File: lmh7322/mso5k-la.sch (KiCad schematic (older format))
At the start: 4 parts, among them J1 output, J2 input

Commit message: Minor cleanup
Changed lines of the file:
@@
 Wire Wire Line
 	3650 4450 3800 4450
-Text GLabel 4550 4400 0    50   Input ~ 0
+Text GLabel 4500 4400 0    50   Input ~ 0
 In8
-Text GLabel 4550 4550 0    50   Input ~ 0
+Text GLabel 4500 4550 0    50   Input ~ 0
 In9
 Wire Wire Line
-	4550 4400 4700 4400
-Wire Wire Line
-	4550 4550 4700 4550
-Text GLabel 4550 5700 0    50   Input ~ 0
+	4500 4400 4650 4400
+Wire Wire Line
+	4500 4550 4650 4550
+Text GLabel 4500 5700 0    50   Input ~ 0
 In10
-Text GLabel 4550 5850 0    50   Input ~ 0
+Text GLabel 4500 5850 0    50   Input ~ 0
 In11
 Wire Wire Line
-	4700 5700 4550 5700
-Wire Wire Line
-	4700 5850 4550 5850
-Text GLabel 5400 4700 2    50   Input ~ 0
+	4650 5700 4500 5700
+Wire Wire Line
+	4650 5850 4500 5850
+Text GLabel 5350 4700 2    50   Input ~ 0
 D9
-Text GLabel 5400 4800 2    50   Input ~ 0
+Text GLabel 5350 4800 2    50   Input ~ 0
 ~D9
-Text GLabel 5400 4450 2    50   Input ~ 0
+Text GLabel 5350 4450 2    50   Input ~ 0
 D8
-Text GLabel 5400 4550 2    50   Input ~ 0
+Text GLabel 5350 4550 2    50   Input ~ 0
 ~D8
-Text GLabel 5400 6000 2    50   Input ~ 0
+Text GLabel 5350 6000 2    50   Input ~ 0
 D11
-Text GLabel 5400 6100 2    50   Input ~ 0
+Text GLabel 5350 6100 2    50   Input ~ 0
 ~D11
-Text GLabel 5400 5750 2    50   Input ~ 0
+Text GLabel 5350 5750 2    50   Input ~ 0
 D10
-Text GLabel 5400 5850 2    50   Input ~ 0
+Text GLabel 5350 5850 2    50   Input ~ 0
 ~D10
 Wire Wire Line
-	5400 6100 5250 6100
-Wire Wire Line
-	5250 6000 5400 6000
-Wire Wire Line
-	5400 5850 5250 5850
-Wire Wire Line
-	5250 5750 5400 5750
-Wire Wire Line
-	5400 4800 5250 4800
-Wire Wire Line
-	5250 4700 5400 4700
-Wire Wire Line
-	5400 4550 5250 4550
-Wire Wire Line
-	5250 4450 5400 4450
-Text GLabel 6350 4400 0    50   Input ~ 0
+	5350 6100 5200 6100
+Wire Wire Line
+	5200 6000 5350 6000
+Wire Wire Line
+	5350 5850 5200 5850
+Wire Wire Line
+	5200 5750 5350 5750
+Wire Wire Line
+	5350 4800 5200 4800
+Wire Wire Line
+	5200 4700 5350 4700
+Wire Wire Line
+	5350 4550 5200 4550
+Wire Wire Line
+	5200 4450 5350 4450
+Text GLabel 6050 4400 0    50   Input ~ 0
 In12
-Text GLabel 6350 4550 0    50   Input ~ 0
+Text GLabel 6050 4550 0    50   Input ~ 0
 In13
 Wire Wire Line
-	6350 4400 6500 4400
-Wire Wire Line
-	6350 4550 6500 4550
-Text GLabel 6350 5700 0    50   Input ~ 0
+	6050 4400 6200 4400
+Wire Wire Line
+	6050 4550 6200 4550
+Text GLabel 6050 5700 0    50   Input ~ 0
 In14
-Text GLabel 6350 5850 0    50   Input ~ 0
+Text GLabel 6050 5850 0    50   Input ~ 0
 In15
 Wire Wire Line
-	6500 5700 6350 5700
-Wire Wire Line
-	6500 5850 6350 5850
-Text GLabel 7200 4700 2    50   Input ~ 0
+	6200 5700 6050 5700
+Wire Wire Line
+	6200 5850 6050 5850
+Text GLabel 6900 4700 2    50   Input ~ 0
 D13
-Text GLabel 7200 4800 2    50   Input ~ 0
+Text GLabel 6900 4800 2    50   Input ~ 0
 ~D13
-Text GLabel 7200 4450 2    50   Input ~ 0
+Text GLabel 6900 4450 2    50   Input ~ 0
 D12
-Text GLabel 7200 4550 2    50   Input ~ 0
+Text GLabel 6900 4550 2    50   Input ~ 0
 ~D12
-Text GLabel 7200 6000 2    50   Input ~ 0
+Text GLabel 6900 6000 2    50   Input ~ 0
 D15
-Text GLabel 7200 6100 2    50   Input ~ 0
+Text GLabel 6900 6100 2    50   Input ~ 0
 ~D15
-Text GLabel 7200 5750 2    50   Input ~ 0
+Text GLabel 6900 5750 2    50   Input ~ 0
 D14
-Text GLabel 7200 5850 2    50   Input ~ 0
+Text GLabel 6900 5850 2    50   Input ~ 0
 ~D14
 Wire Wire Line
-	7200 6100 7050 6100
-Wire Wire Line
-	7050 6000 7200 6000
-Wire Wire Line
-	7200 5850 7050 5850
-Wire Wire Line
-	7050 5750 7200 5750
-Wire Wire Line
-	7200 4800 7050 4800
-Wire Wire Line
-	7050 4700 7200 4700
-Wire Wire Line
-	7200 4550 7050 4550
-Wire Wire Line
-	7050 4450 7200 4450
+	6900 6100 6750 6100
+Wire Wire Line
+	6750 6000 6900 6000
+Wire Wire Line
+	6900 5850 6750 5850
+Wire Wire Line
+	6750 5750 6900 5750
+Wire Wire Line
+	6900 4800 6750 4800
+Wire Wire Line
+	6750 4700 6900 4700
+Wire Wire Line
+	6900 4550 6750 4550
+Wire Wire Line
+	6750 4450 6900 4450
 Text GLabel 1450 6050 0    50   Input ~ 0
 Vref_0-7
@@
 Wire Wire Line
 	3100 6050 2950 6050
-Text GLabel 4550 6050 0    50   Input ~ 0
+Text GLabel 4500 6050 0    50   Input ~ 0
 Vref_8-15
-Text GLabel 6350 6050 0    50   Input ~ 0
+Text GLabel 6050 6050 0    50   Input ~ 0
 Vref_8-15
 Wire Wire Line
-	6350 6050 6500 6050
-Wire Wire Line
-	4700 6050 4550 6050
+	6050 6050 6200 6050
+Wire Wire Line
+	4650 6050 4500 6050
 Text Notes 1050 3950 0    50   ~ 0
 For reference see:\nhttp://www.eevblog.com/forum/testgear/hacking-the-rigol-mso5000-series-oscilloscopes/msg2057401/#msg2057401
@@
 $EndSheet
 $Sheet
-S 4700 5600 550  650
+S 4650 5600 550  650
 U 5C4E2524
 F0 "ch 10-11" 50
 F1 "dual.sch" 50
-F2 "InB" I L 4700 5850 50
-F3 "Vref" I L 4700 6050 50
-F4 "OutA" I R 5250 5750 50
-F5 "~OutA" I R 5250 5850 50
-F6 "InA" I L 4700 5700 50
-F7 "OutB" I R 5250 6000 50
-F8 "~OutB" I R 5250 6100 50
-$EndSheet
-$Sheet
-S 4700 4300 550  650
+F2 "InB" I L 4650 5850 50
+F3 "Vref" I L 4650 6050 50
+F4 "OutA" I R 5200 5750 50
+F5 "~OutA" I R 5200 5850 50
+F6 "InA" I L 4650 5700 50
+F7 "OutB" I R 5200 6000 50
+F8 "~OutB" I R 5200 6100 50
+$EndSheet
+$Sheet
+S 4650 4300 550  650
 U 5C4E98BE
 F0 "ch 8-9" 50
 F1 "dual.sch" 50
-F2 "InB" I L 4700 4550 50
-F3 "Vref" I L 4700 4750 50
-F4 "OutA" I R 5250 4450 50
-F5 "~OutA" I R 5250 4550 50
-F6 "InA" I L 4700 4400 50
-F7 "OutB" I R 5250 4700 50
-F8 "~OutB" I R 5250 4800 50
-$EndSheet
-$Sheet
-S 6500 4300 550  650
+F2 "InB" I L 4650 4550 50
+F3 "Vref" I L 4650 4750 50
+F4 "OutA" I R 5200 4450 50
+F5 "~OutA" I R 5200 4550 50
+F6 "InA" I L 4650 4400 50
+F7 "OutB" I R 5200 4700 50
+F8 "~OutB" I R 5200 4800 50
+$EndSheet
+$Sheet
+S 6200 4300 550  650
 U 5C4E98C7
 F0 "ch 12-13" 50
 F1 "dual.sch" 50
-F2 "InB" I L 6500 4550 50
-F3 "Vref" I L 6500 4750 50
-F4 "OutA" I R 7050 4450 50
-F5 "~OutA" I R 7050 4550 50
-F6 "InA" I L 6500 4400 50
-F7 "OutB" I R 7050 4700 50
-F8 "~OutB" I R 7050 4800 50
-$EndSheet
-$Sheet
-S 6500 5600 550  650
+F2 "InB" I L 6200 4550 50
+F3 "Vref" I L 6200 4750 50
+F4 "OutA" I R 6750 4450 50
+F5 "~OutA" I R 6750 4550 50
+F6 "InA" I L 6200 4400 50
+F7 "OutB" I R 6750 4700 50
+F8 "~OutB" I R 6750 4800 50
+$EndSheet
+$Sheet
+S 6200 5600 550  650
 U 5C4E98D0
 F0 "ch 14-15" 50
 F1 "dual.sch" 50
-F2 "InB" I L 6500 5850 50
-F3 "Vref" I L 6500 6050 50
-F4 "OutA" I R 7050 5750 50
-F5 "~OutA" I R 7050 5850 50
-F6 "InA" I L 6500 5700 50
-F7 "OutB" I R 7050 6000 50
-F8 "~OutB" I R 7050 6100 50
+F2 "InB" I L 6200 5850 50
+F3 "Vref" I L 6200 6050 50
+F4 "OutA" I R 6750 5750 50
+F5 "~OutA" I R 6750 5850 50
+F6 "InA" I L 6200 5700 50
+F7 "OutB" I R 6750 6000 50
+F8 "~OutB" I R 6750 6100 50
 $EndSheet
 Text GLabel 2950 4750 0    50   Input ~ 0
@@
 Wire Wire Line
 	2950 4750 3100 4750
-Text GLabel 4550 4750 0    50   Input ~ 0
+Text GLabel 4500 4750 0    50   Input ~ 0
 Vref_8-15
 Wire Wire Line
-	4550 4750 4700 4750
-Text GLabel 6350 4750 0    50   Input ~ 0
+	4500 4750 4650 4750
+Text GLabel 6050 4750 0    50   Input ~ 0
 Vref_8-15
 Wire Wire Line
-	6350 4750 6500 4750
+	6050 4750 6200 4750
 $EndSCHEMATC

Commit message: Started playing around with the PCB layout
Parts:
- added C13, C14, C15: 10uF, Capacitors_SMD.pretty:C_1206_HandSoldering, symbol Device:C
- added C16: 100n, Capacitors_SMD.pretty:C_0603_HandSoldering, symbol Device:C
- J1: footprint (none) -> Connectors_IDC.pretty:IDC-Header_2x25_Pitch2.54mm_Angled
- J2: footprint (none) -> Connector_PinHeader_2.54mm:PinHeader_1x17_P2.54mm_Horizontal
- R1, R2: footprint (none) -> Resistor_SMD:R_0603_1608Metric_Pad1.05x0.95mm_HandSolder
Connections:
- net +2V5: now also C14.1
- net +4V: now also C13.1
- net -2V5: now also C15.1
- net GND: now also C13.2, C14.2, C15.2, C16.2
- new net Vref: C16.1
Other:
- moved on the sheet: R1, R2

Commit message: Pre-clone
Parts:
- renumbered C13 to C101, C14 to C102, C15 to C103, C16 to C104, J1 to J101, J2 to J102, R1 to R101, R2 to R102

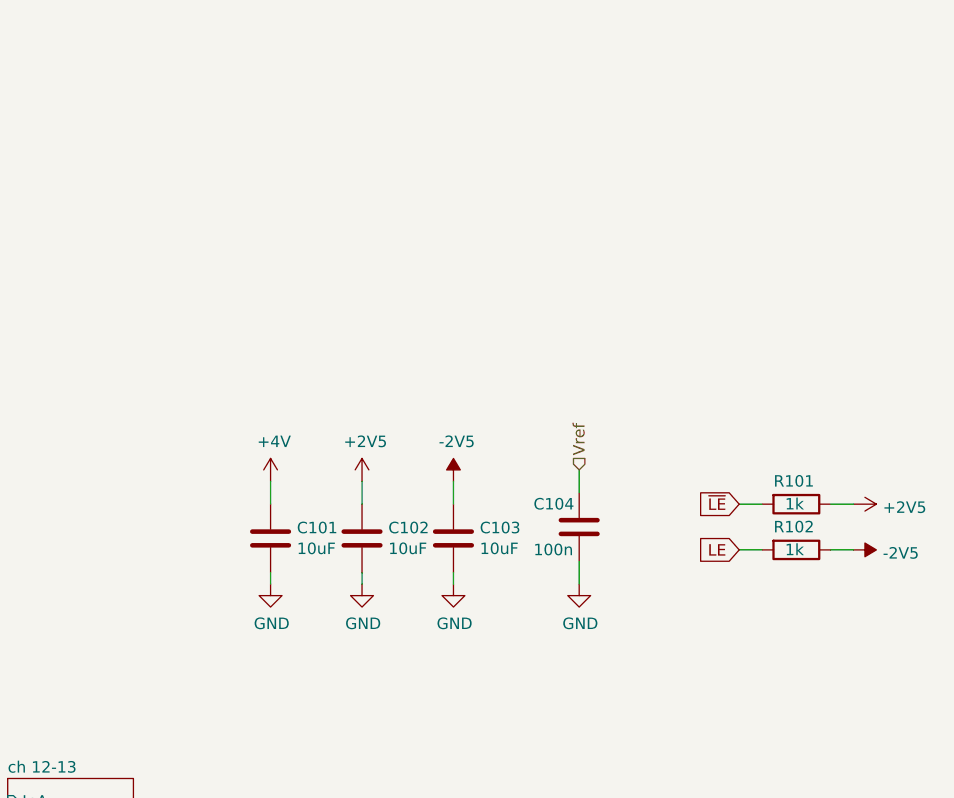
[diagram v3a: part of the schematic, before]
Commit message: Finished the 4-layer single-sided board
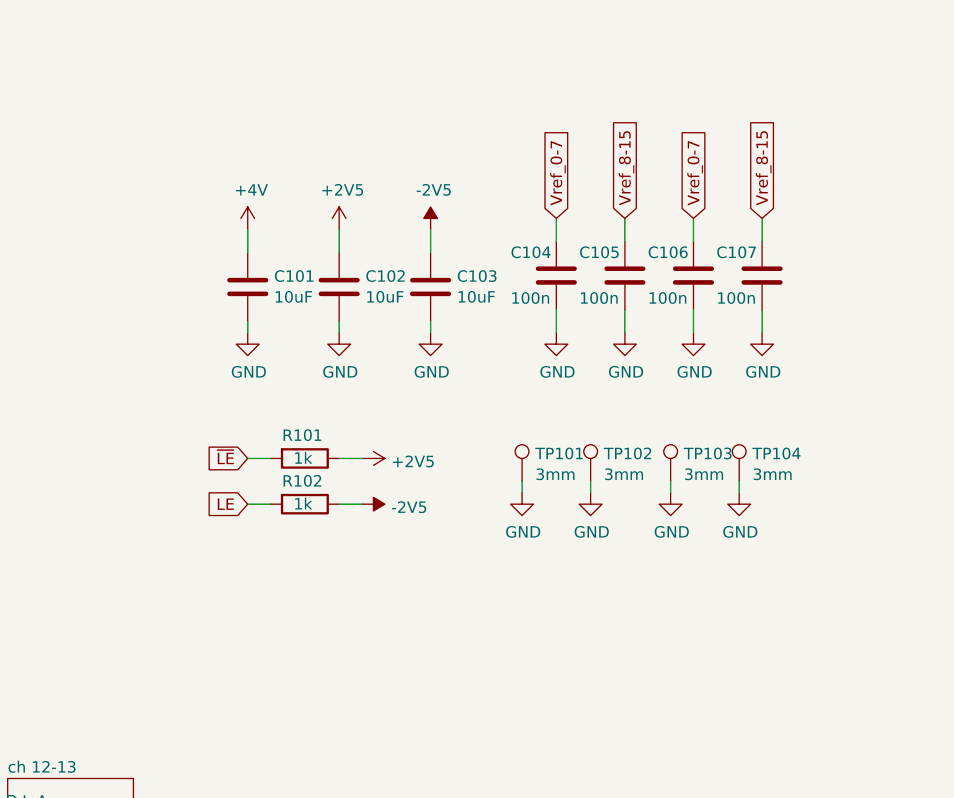
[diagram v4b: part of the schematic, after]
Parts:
- added C105, C106, C107: 100n, Capacitors_SMD.pretty:C_0603_HandSoldering, symbol Device:C
- added TP101, TP102, TP103, TP104: 3mm, lmh7322:3mm, symbol Connector:TestPoint
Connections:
- net Vref is gone; now on net Vref_0-7: C104.1
- net GND: now also C105.2, C106.2, C107.2, TP101.1, TP102.1, TP103.1, TP104.1
- net Vref_0-7: now also C106.1
- net Vref_8-15: now also C105.1, C107.1
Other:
- moved on the sheet: C101, C102, C103, C104, R101, R102
